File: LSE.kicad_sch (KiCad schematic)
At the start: 5 parts, among them Y2 32.758kHz

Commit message: converted R, C, and L to smaller 0402 footprints. Some trace rearranging and cleanup.
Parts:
- C12, C13: footprint ProjectLib:C_0603_1608Metric -> ProjectLib:C_0402_1005Metric; Manufacturer TDK Corp -> (none); MfgPart CGA3E2C0G1H040CT0Y0N -> (none); Package C_0603_1608Metric -> C_0402_1005Metric
- R29: footprint ProjectLib:R_0603_1608Metric -> ProjectLib:R_0402_1005Metric; Manufacturer Yageo -> (none); MfgPart RC0603FR-070RL -> (none); Package R_0603_1608Metric -> R_0402_1005Metric
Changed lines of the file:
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@@
 			)
 		)
-		(property "Footprint" "ProjectLib:C_0603_1608Metric"
+		(property "Footprint" "ProjectLib:C_0402_1005Metric"
 			(at 128.5748 101.6 0)
 			(effects
@@
 			)
 		)
-		(property "Manufacturer" "TDK Corp"
-			(at 129.54 105.41 0)
-			(effects
-				(font
-					(size 1.27 1.27)
-				)
-				(hide yes)
-			)
-		)
-		(property "MfgPart" "CGA3E2C0G1H040CT0Y0N"
-			(at 129.54 105.41 0)
-			(effects
-				(font
-					(size 1.27 1.27)
-				)
-				(hide yes)
-			)
-		)
-		(property "Package" "C_0603_1608Metric"
+		(property "Manufacturer" ""
+			(at 129.54 105.41 0)
+			(effects
+				(font
+					(size 1.27 1.27)
+				)
+				(hide yes)
+			)
+		)
+		(property "MfgPart" ""
+			(at 129.54 105.41 0)
+			(effects
+				(font
+					(size 1.27 1.27)
+				)
+				(hide yes)
+			)
+		)
+		(property "Package" "C_0402_1005Metric"
 			(at 129.54 105.41 0)
 			(effects
@@
 			)
 		)
-		(property "Footprint" "ProjectLib:C_0603_1608Metric"
+		(property "Footprint" "ProjectLib:C_0402_1005Metric"
 			(at 112.0648 101.6 0)
 			(effects
@@
 			)
 		)
-		(property "Manufacturer" "TDK Corp"
-			(at 113.03 105.41 0)
-			(effects
-				(font
-					(size 1.27 1.27)
-				)
-				(hide yes)
-			)
-		)
-		(property "MfgPart" "CGA3E2C0G1H040CT0Y0N"
-			(at 113.03 105.41 0)
-			(effects
-				(font
-					(size 1.27 1.27)
-				)
-				(hide yes)
-			)
-		)
-		(property "Package" "C_0603_1608Metric"
+		(property "Manufacturer" ""
+			(at 113.03 105.41 0)
+			(effects
+				(font
+					(size 1.27 1.27)
+				)
+				(hide yes)
+			)
+		)
+		(property "MfgPart" ""
+			(at 113.03 105.41 0)
+			(effects
+				(font
+					(size 1.27 1.27)
+				)
+				(hide yes)
+			)
+		)
+		(property "Package" "C_0402_1005Metric"
 			(at 113.03 105.41 0)
 			(effects
@@
 			)
 		)
-		(property "Footprint" "ProjectLib:R_0603_1608Metric"
+		(property "Footprint" "ProjectLib:R_0402_1005Metric"
 			(at 130.556 85.344 90)
 			(effects
@@
 			)
 		)
-		(property "Manufacturer" "Yageo"
-			(at 129.54 85.09 0)
-			(effects
-				(font
-					(size 1.27 1.27)
-				)
-				(hide yes)
-			)
-		)
-		(property "MfgPart" "RC0603FR-070RL"
-			(at 129.54 85.09 0)
-			(effects
-				(font
-					(size 1.27 1.27)
-				)
-				(hide yes)
-			)
-		)
-		(property "Package" "R_0603_1608Metric"
-			(at 129.54 85.09 0)
-			(effects
+		(property "Manufacturer" ""
+			(at 129.54 85.09 0)
+			(effects
+				(font
+					(size 1.27 1.27)
+				)
+				(hide yes)
+			)
+		)
+		(property "MfgPart" ""
+			(at 129.54 85.09 0)
+			(effects
+				(font
+					(size 1.27 1.27)
+				)
+				(hide yes)
+			)
+		)
+		(property "Package" "R_0402_1005Metric"
+			(at 129.54 85.09 0)
+			(effects

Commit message: improved schematic sheet titles.
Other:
- title: ADCs for 10K thermistors -> LSE
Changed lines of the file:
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@@
 	(paper "A4")
 	(title_block
-		(title "ADCs for 10K thermistors")
-		(date "2025-01-07")
-		(rev "v0.1.1")
+		(title "LSE")
+		(date "2025-09-15")
+		(rev "v0.2.2")
 	)
 	(junction

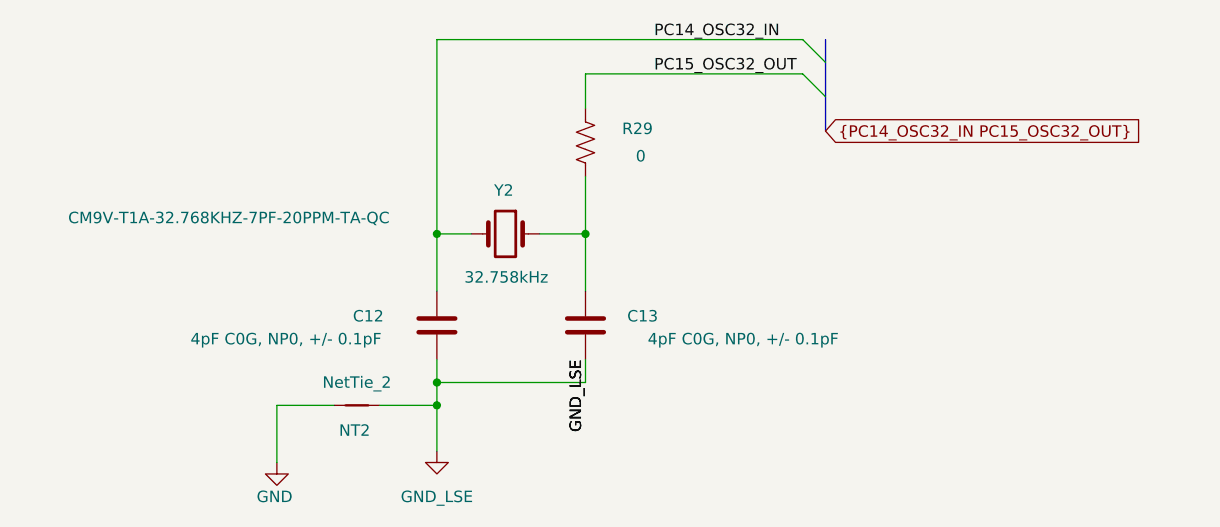
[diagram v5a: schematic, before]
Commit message: added QR and ID blocks on silkscreen. Marked HSE and LSE as DNP. Revised version number to 0.3.1.
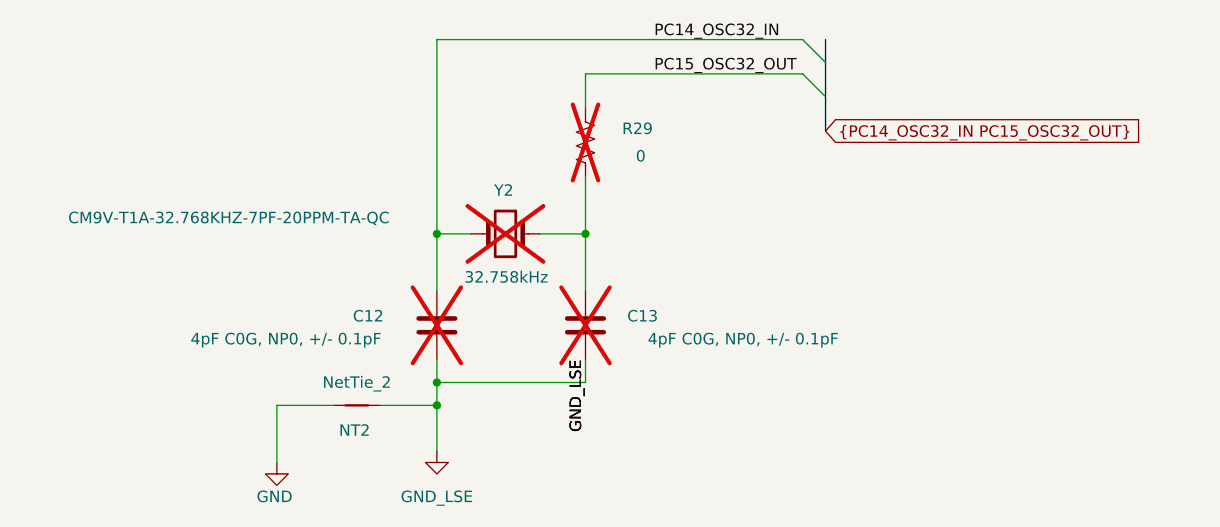
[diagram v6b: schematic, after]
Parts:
- C12, C13, R29, Y2: now not fitted
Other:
- title: LSE -> stm32f411, RFM95W
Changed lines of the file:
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@@
 	(paper "A4")
 	(title_block
-		(title "LSE")
-		(date "2025-09-15")
-		(rev "v0.2.2")
+		(title "stm32f411, RFM95W")
+		(date "2026-04-12")
+		(rev "v0.3.1")
 	)
 	(junction
@@
 		(in_bom yes)
 		(on_board yes)
-		(in_pos_files yes)
-		(dnp no)
+		(in_pos_files no)
+		(dnp yes)
 		(property "Reference" "C13"
 			(at 135.89 104.394 0)
@@
 		(in_bom yes)
 		(on_board yes)
-		(in_pos_files yes)
-		(dnp no)
+		(in_pos_files no)
+		(dnp yes)
 		(property "Reference" "C12"
 			(at 105.41 104.394 0)
@@
 		(in_bom yes)
 		(on_board yes)
-		(in_pos_files yes)
-		(dnp no)
+		(in_pos_files no)
+		(dnp yes)
 		(property "Reference" "R29"
 			(at 133.604 83.566 0)
@@
 		(in_bom yes)
 		(on_board yes)
-		(in_pos_files yes)
-		(dnp no)
+		(in_pos_files no)
+		(dnp yes)
 		(property "Reference" "Y2"
 			(at 119.38 90.424 0)
